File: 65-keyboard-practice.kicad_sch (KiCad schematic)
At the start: 3 parts

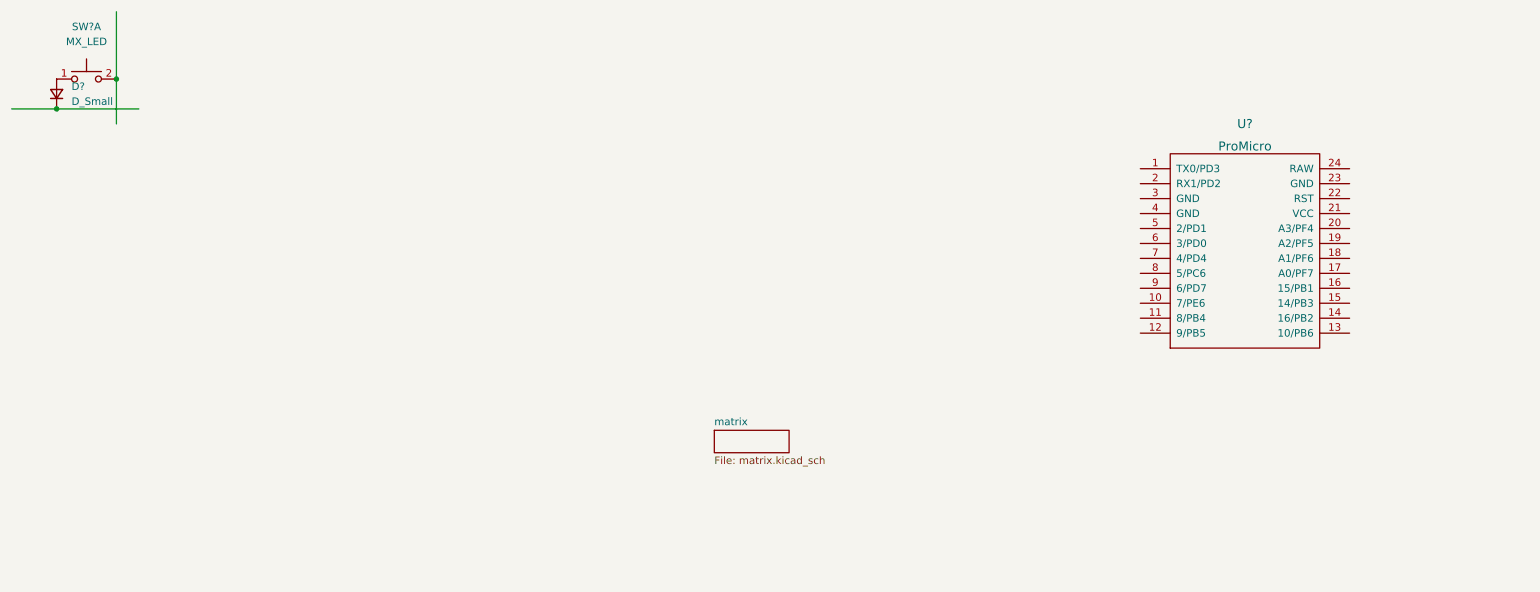
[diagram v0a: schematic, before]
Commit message: added GND and reset button to the promicro
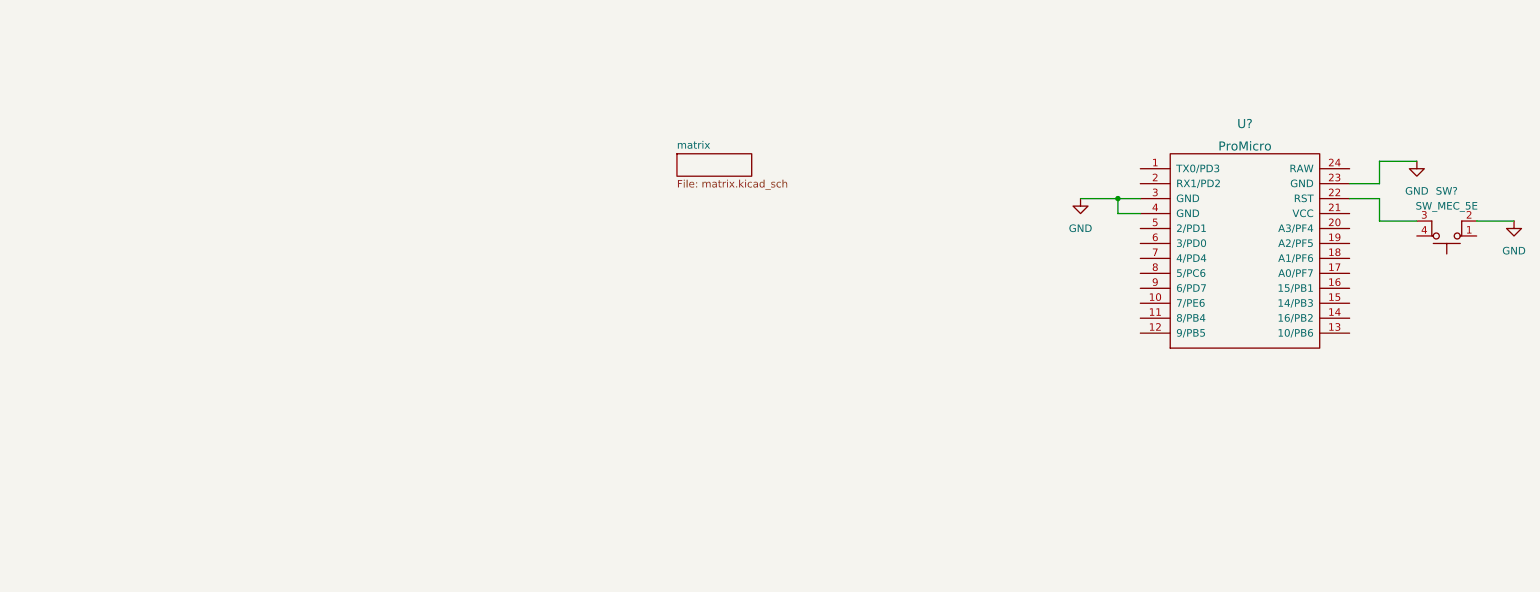
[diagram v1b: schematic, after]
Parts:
- removed D?: D_Small, symbol Device:D_Small
- removed SW?: MX_LED, symbol keebio:MX_LED
- added SW?: SW_MEC_5E, symbol Switch:SW_MEC_5E
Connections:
- net at U?.22 (RST): now also SW?.3 (K)
- net GND: now reaches U?.23 (GND)
- net GND: now also U?.3 (GND), U?.4 (GND), SW?.2
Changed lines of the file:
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@@
 (kicad_sch (version 20211123) (generator eeschema)
   (paper "A4")
-  (junction (at 40.64 38.1) (diameter 0) (color 0 0 0 0)
-  )
-  (junction (at 30.48 43.18) (diameter 0) (color 0 0 0 0)
-  )
-  (wire (pts (xy 22.86 43.18) (xy 30.48 43.18))
-    (stroke (width 0) (type default) (color 0 0 0 0))
-  )
-  (wire (pts (xy 30.48 43.18) (xy 44.45 43.18))
-    (stroke (width 0) (type default) (color 0 0 0 0))
-  )
-  (wire (pts (xy 40.64 26.67) (xy 40.64 38.1))
-    (stroke (width 0) (type default) (color 0 0 0 0))
-  )
-  (wire (pts (xy 40.64 38.1) (xy 40.64 45.72))
-    (stroke (width 0) (type default) (color 0 0 0 0))
-  )
-  (symbol (lib_id "keebio:MX_LED") (at 35.56 38.1 0) (unit 1)
+  (junction (at 210.82 58.42) (diameter 0) (color 0 0 0 0)
+  )
+  (wire (pts (xy 255.27 58.42) (xy 255.27 62.23))
+    (stroke (width 0) (type default) (color 0 0 0 0))
+  )
+  (wire (pts (xy 250.19 55.88) (xy 255.27 55.88))
+    (stroke (width 0) (type default) (color 0 0 0 0))
+  )
+  (wire (pts (xy 255.27 62.23) (xy 261.62 62.23))
+    (stroke (width 0) (type default) (color 0 0 0 0))
+  )
+  (wire (pts (xy 255.27 55.88) (xy 255.27 52.07))
+    (stroke (width 0) (type default) (color 0 0 0 0))
+  )
+  (wire (pts (xy 255.27 52.07) (xy 261.62 52.07))
+    (stroke (width 0) (type default) (color 0 0 0 0))
+  )
+  (wire (pts (xy 204.47 58.42) (xy 210.82 58.42))
+    (stroke (width 0) (type default) (color 0 0 0 0))
+  )
+  (wire (pts (xy 271.78 62.23) (xy 278.13 62.23))
+    (stroke (width 0) (type default) (color 0 0 0 0))
+  )
+  (wire (pts (xy 210.82 58.42) (xy 214.63 58.42))
+    (stroke (width 0) (type default) (color 0 0 0 0))
+  )
+  (wire (pts (xy 250.19 58.42) (xy 255.27 58.42))
+    (stroke (width 0) (type default) (color 0 0 0 0))
+  )
+  (wire (pts (xy 210.82 60.96) (xy 210.82 58.42))
+    (stroke (width 0) (type default) (color 0 0 0 0))
+  )
+  (wire (pts (xy 214.63 60.96) (xy 210.82 60.96))
+    (stroke (width 0) (type default) (color 0 0 0 0))
+  )
+  (symbol (lib_id "power:GND") (at 204.47 58.42 0) (unit 1)
     (in_bom yes) (on_board yes) (fields_autoplaced)
-    (property "Reference" "SW?" (id 0) (at 35.56 29.21 0))
-    (property "Value" "MX_LED" (id 1) (at 35.56 31.75 0))
-    (property "Footprint" "" (id 2) (at 35.56 38.1 0)
-      (effects (font (size 1.27 1.27)) hide)
-    )
-    (property "Datasheet" "" (id 3) (at 35.56 38.1 0)
+    (property "Reference" "#PWR?" (id 0) (at 204.47 64.77 0)
+      (effects (font (size 1.27 1.27)) hide)
+    )
+    (property "Value" "GND" (id 1) (at 204.47 63.5 0))
+    (property "Footprint" "" (id 2) (at 204.47 58.42 0)
+      (effects (font (size 1.27 1.27)) hide)
+    )
+    (property "Datasheet" "" (id 3) (at 204.47 58.42 0)
+      (effects (font (size 1.27 1.27)) hide)
+    )
+    (pin "1")
+  )
+  (symbol (lib_id "Switch:SW_MEC_5E") (at 266.7 62.23 180) (unit 1)
+    (in_bom yes) (on_board yes) (fields_autoplaced)
+    (property "Reference" "SW?" (id 0) (at 266.7 57.15 0))
+    (property "Value" "SW_MEC_5E" (id 1) (at 266.7 59.69 0))
+    (property "Footprint" "" (id 2) (at 266.7 69.85 0)
+      (effects (font (size 1.27 1.27)) hide)
+    )
+    (property "Datasheet" "http://www.apem.com/int/index.php?controller=attachment&id_attachment=1371" (id 3) (at 266.7 69.85 0)
       (effects (font (size 1.27 1.27)) hide)
     )
@@
     (pin "4")
   )
-  (symbol (lib_id "Device:D_Small") (at 30.48 40.64 90) (unit 1)
+  (symbol (lib_id "power:GND") (at 261.62 52.07 0) (unit 1)
     (in_bom yes) (on_board yes) (fields_autoplaced)
-    (property "Reference" "D?" (id 0) (at 33.02 39.3699 90)
-      (effects (font (size 1.27 1.27)) (justify right))
-    )
-    (property "Value" "D_Small" (id 1) (at 33.02 41.9099 90)
-      (effects (font (size 1.27 1.27)) (justify right))
-    )
-    (property "Footprint" "" (id 2) (at 30.48 40.64 90)
-      (effects (font (size 1.27 1.27)) hide)
-    )
-    (property "Datasheet" "~" (id 3) (at 30.48 40.64 90)
+    (property "Reference" "#PWR?" (id 0) (at 261.62 58.42 0)
+      (effects (font (size 1.27 1.27)) hide)
+    )
+    (property "Value" "GND" (id 1) (at 261.62 57.15 0))
+    (property "Footprint" "" (id 2) (at 261.62 52.07 0)
+      (effects (font (size 1.27 1.27)) hide)
+    )
+    (property "Datasheet" "" (id 3) (at 261.62 52.07 0)
       (effects (font (size 1.27 1.27)) hide)
     )
     (pin "1")
-    (pin "2")
   )
   (symbol (lib_id "keebio:ProMicro") (at 232.41 67.31 0) (unit 1)
@@
     (pin "9")
   )
-  (sheet (at 142.24 97.79) (size 12.7 3.81) (fields_autoplaced)
+  (symbol (lib_id "power:GND") (at 278.13 62.23 0) (unit 1)
+    (in_bom yes) (on_board yes) (fields_autoplaced)
+    (property "Reference" "#PWR?" (id 0) (at 278.13 68.58 0)
+      (effects (font (size 1.27 1.27)) hide)
+    )
+    (property "Value" "GND" (id 1) (at 278.13 67.31 0))
+    (property "Footprint" "" (id 2) (at 278.13 62.23 0)
+      (effects (font (size 1.27 1.27)) hide)
+    )
+    (property "Datasheet" "" (id 3) (at 278.13 62.23 0)
+      (effects (font (size 1.27 1.27)) hide)
+    )
+    (pin "1")
+  )
+  (sheet (at 135.89 50.8) (size 12.7 3.81) (fields_autoplaced)
     (stroke (width 0.1524) (type solid) (color 0 0 0 0))
     (fill (color 0 0 0 0.0000))
-    (property "Sheet name" "matrix" (id 0) (at 142.24 97.0784 0)
+    (property "Sheet name" "matrix" (id 0) (at 135.89 50.0884 0)
       (effects (font (size 1.27 1.27)) (justify left bottom))
     )
-    (property "Sheet file" "matrix.kicad_sch" (id 1) (at 142.24 102.1846 0)
+    (property "Sheet file" "matrix.kicad_sch" (id 1) (at 135.89 55.1946 0)
       (effects (font (size 1.27 1.27)) (justify left top))
     )
@@
   )
   (symbol_instances
+    (path "/73fcfd8a-9610-4862-8758-a9cb100236aa"
+      (reference "#PWR?") (unit 1) (value "GND") (footprint "")
+    )
+    (path "/9c7935a6-744f-46b1-a276-27252c39d402"
+      (reference "#PWR?") (unit 1) (value "GND") (footprint "")
+    )
+    (path "/f2ebe5e8-f267-4b40-9cca-169b4324c72b"
+      (reference "#PWR?") (unit 1) (value "GND") (footprint "")
+    )
     (path "/c4ed3659-6d37-44a6-b5ca-7e464c3558fc/0189b339-e276-445f-84b3-11fa3e094def"
       (reference "D?") (unit 1) (value "D_Small") (footprint "")
@@
       (reference "D?") (unit 1) (value "D_Small") (footprint "")
     )
-    (path "/b217ac5c-bb08-4598-80a1-f708d8012252"
-      (reference "D?") (unit 1) (value "D_Small") (footprint "")
-    )
     (path "/c4ed3659-6d37-44a6-b5ca-7e464c3558fc/b26f658e-15d8-48fa-af25-636915254238"
       (reference "D?") (unit 1) (value "D_Small") (footprint "")
@@
       (reference "SW?") (unit 1) (value "MX_LED") (footprint "")
     )
-    (path "/7689c30f-813f-42a7-ad77-22c5cfc89d79"
-      (reference "SW?") (unit 1) (value "MX_LED") (footprint "")
+    (path "/76c93b00-4581-47e2-860e-798daded2dfe"
+      (reference "SW?") (unit 1) (value "SW_MEC_5E") (footprint "")
     )
     (path "/c4ed3659-6d37-44a6-b5ca-7e464c3558fc/855e7ffd-9a29-4ac3-92c9-7962e6bb0d8f"

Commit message: added some submodules
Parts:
- gave numbers to parts that had none: 2

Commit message: half wiring done
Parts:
- SW1: footprint (none) -> random-keyboard-parts:PushButton_6x6mm_TH
- U1: footprint (none) -> Keebio-Parts:ArduinoProMicro

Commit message: Finished the design
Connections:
- net COL1: now reaches U1.10 (7/PE6)
- net COL2: now reaches U1.11 (8/PB4)
- net COL3: now reaches U1.12 (9/PB5)
- net COL4: now reaches U1.13 (10/PB6)
- net COL5: now reaches U1.14 (16/PB2)
- net COL6: now reaches U1.15 (14/PB3)
- net COL7: now reaches U1.16 (15/PB1)
- net ROW4: now reaches U1.17 (A0/PF7)
- net ROW3: now reaches U1.5 (2/PD1)
- net ROW2: now reaches U1.6 (3/PD0)
- net ROW0: now reaches U1.7 (4/PD4)
- net ROW1: now reaches U1.8 (5/PC6)
- net COL0: now reaches U1.9 (6/PD7)
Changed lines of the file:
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@@
     (stroke (width 0) (type default) (color 0 0 0 0))
+  )
+  (global_label "ROW1" (shape input) (at 214.63 71.12 180) (fields_autoplaced)
+    (effects (font (size 1.27 1.27)) (justify right))
+    (property "Intersheet References" "${INTERSHEET_REFS}" (id 0) (at 206.9555 71.0406 0)
+      (effects (font (size 1.27 1.27)) (justify right) hide)
+    )
+  )
+  (global_label "ROW4" (shape input) (at 250.19 71.12 0) (fields_autoplaced)
+    (effects (font (size 1.27 1.27)) (justify left))
+    (property "Intersheet References" "${INTERSHEET_REFS}" (id 0) (at 257.8645 71.0406 0)
+      (effects (font (size 1.27 1.27)) (justify left) hide)
+    )
+  )
+  (global_label "COL0" (shape input) (at 214.63 73.66 180) (fields_autoplaced)
+    (effects (font (size 1.27 1.27)) (justify right))
+    (property "Intersheet References" "${INTERSHEET_REFS}" (id 0) (at 207.3788 73.5806 0)
+      (effects (font (size 1.27 1.27)) (justify right) hide)
+    )
+  )
+  (global_label "COL2" (shape input) (at 214.63 78.74 180) (fields_autoplaced)
+    (effects (font (size 1.27 1.27)) (justify right))
+    (property "Intersheet References" "${INTERSHEET_REFS}" (id 0) (at 207.3788 78.6606 0)
+      (effects (font (size 1.27 1.27)) (justify right) hide)
+    )
+  )
+  (global_label "ROW0" (shape input) (at 214.63 68.58 180) (fields_autoplaced)
+    (effects (font (size 1.27 1.27)) (justify right))
+    (property "Intersheet References" "${INTERSHEET_REFS}" (id 0) (at 206.9555 68.5006 0)
+      (effects (font (size 1.27 1.27)) (justify right) hide)
+    )
+  )
+  (global_label "COL3" (shape input) (at 214.63 81.28 180) (fields_autoplaced)
+    (effects (font (size 1.27 1.27)) (justify right))
+    (property "Intersheet References" "${INTERSHEET_REFS}" (id 0) (at 207.3788 81.2006 0)
+      (effects (font (size 1.27 1.27)) (justify right) hide)
+    )
+  )
+  (global_label "COL1" (shape input) (at 214.63 76.2 180) (fields_autoplaced)
+    (effects (font (size 1.27 1.27)) (justify right))
+    (property "Intersheet References" "${INTERSHEET_REFS}" (id 0) (at 207.3788 76.1206 0)
+      (effects (font (size 1.27 1.27)) (justify right) hide)
+    )
+  )
+  (global_label "COL4" (shape input) (at 250.19 81.28 0) (fields_autoplaced)
+    (effects (font (size 1.27 1.27)) (justify left))
+    (property "Intersheet References" "${INTERSHEET_REFS}" (id 0) (at 257.4412 81.2006 0)
+      (effects (font (size 1.27 1.27)) (justify left) hide)
+    )
+  )
+  (global_label "ROW3" (shape input) (at 214.63 63.5 180) (fields_autoplaced)
+    (effects (font (size 1.27 1.27)) (justify right))
+    (property "Intersheet References" "${INTERSHEET_REFS}" (id 0) (at 206.9555 63.4206 0)
+      (effects (font (size 1.27 1.27)) (justify right) hide)
+    )
+  )
+  (global_label "COL5" (shape input) (at 250.19 78.74 0) (fields_autoplaced)
+    (effects (font (size 1.27 1.27)) (justify left))
+    (property "Intersheet References" "${INTERSHEET_REFS}" (id 0) (at 257.4412 78.6606 0)
+      (effects (font (size 1.27 1.27)) (justify left) hide)
+    )
+  )
+  (global_label "COL7" (shape input) (at 250.19 73.66 0) (fields_autoplaced)
+    (effects (font (size 1.27 1.27)) (justify left))
+    (property "Intersheet References" "${INTERSHEET_REFS}" (id 0) (at 257.4412 73.5806 0)
+      (effects (font (size 1.27 1.27)) (justify left) hide)
+    )
+  )
+  (global_label "ROW2" (shape input) (at 214.63 66.04 180) (fields_autoplaced)
+    (effects (font (size 1.27 1.27)) (justify right))
+    (property "Intersheet References" "${INTERSHEET_REFS}" (id 0) (at 206.9555 65.9606 0)
+      (effects (font (size 1.27 1.27)) (justify right) hide)
+    )
+  )
+  (global_label "COL6" (shape input) (at 250.19 76.2 0) (fields_autoplaced)
+    (effects (font (size 1.27 1.27)) (justify left))
+    (property "Intersheet References" "${INTERSHEET_REFS}" (id 0) (at 257.4412 76.1206 0)
+      (effects (font (size 1.27 1.27)) (justify left) hide)
+    )
   )
   (symbol (lib_id "power:GND") (at 204.47 58.42 0) (unit 1)

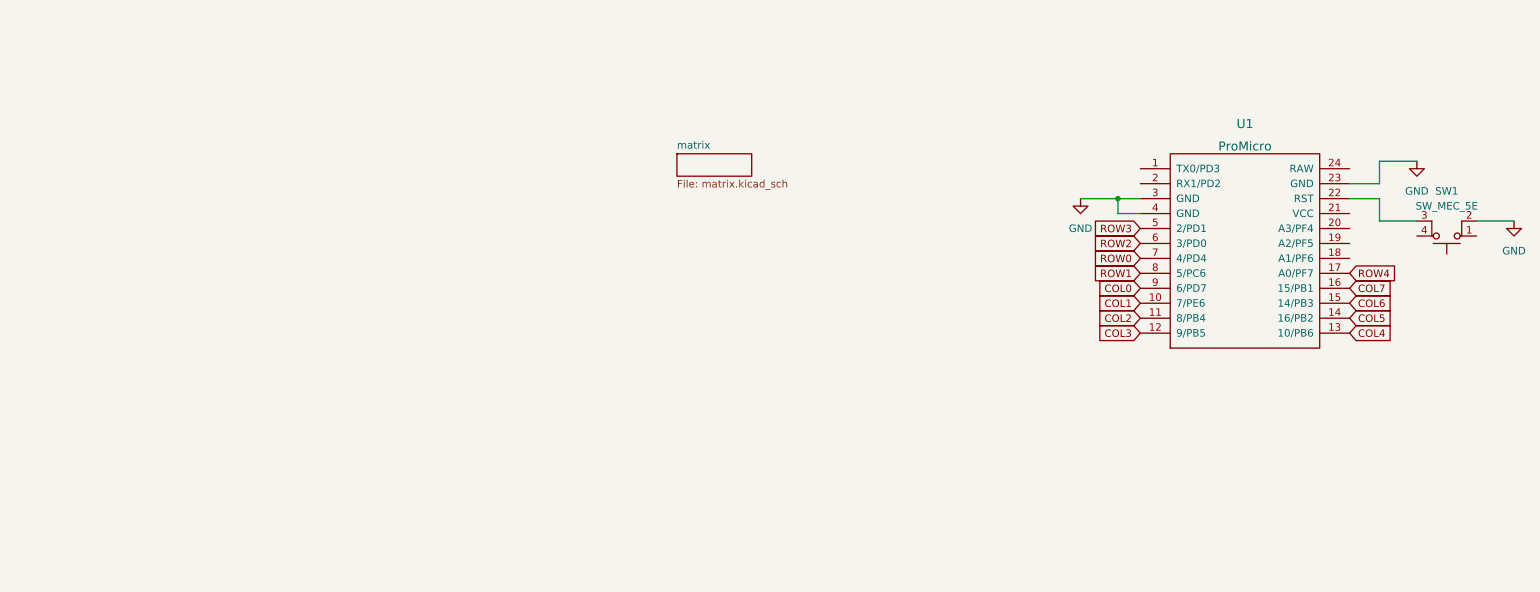
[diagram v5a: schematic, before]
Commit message: Added rgb underglow
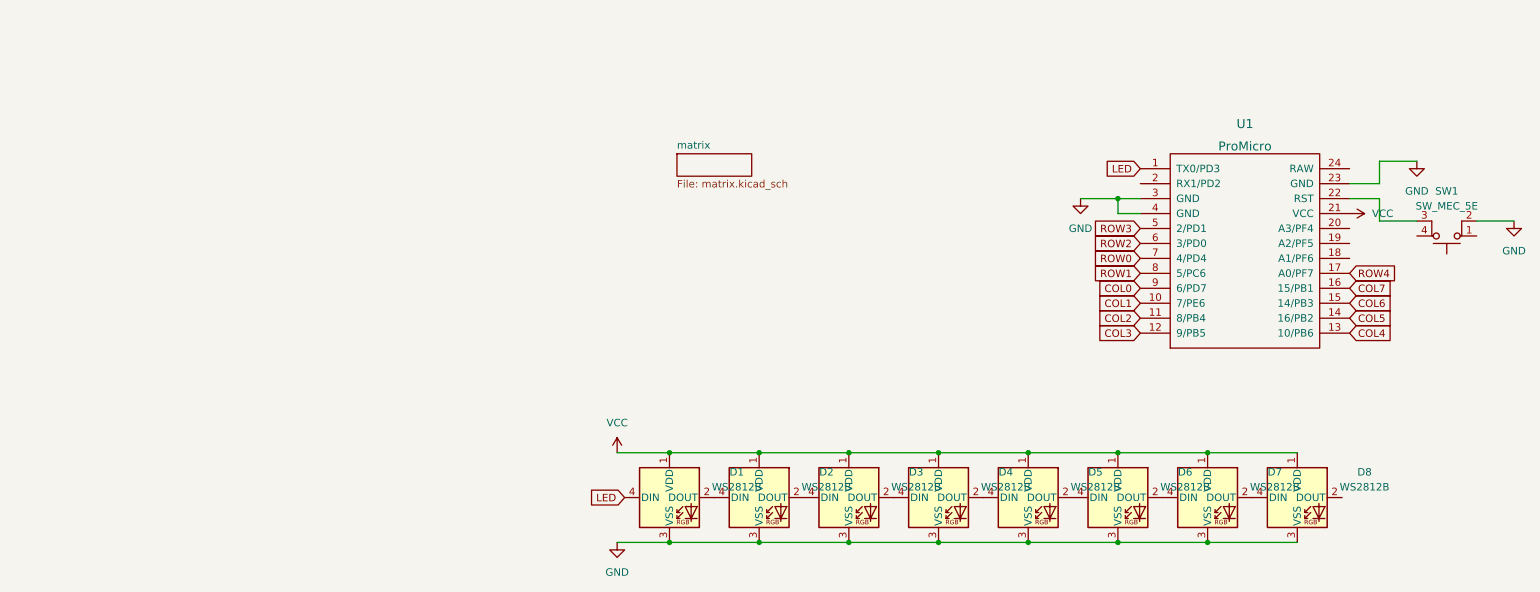
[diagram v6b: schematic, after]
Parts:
- added D1, D2, D3, D4, D5, D6, D7, D8: WS2812B, LED_SMD:LED_WS2812B_PLCC4_5.0x5.0mm_P3.2mm, symbol LED:WS2812B
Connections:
- net GND: now also D1.3 (VSS), D2.3 (VSS), D3.3 (VSS), D4.3 (VSS), D5.3 (VSS), D6.3 (VSS), D7.3 (VSS), D8.3 (VSS)
- net LED: now reaches U1.1 (TX0/PD3)
- net LED: now also D1.4 (DIN)
- net VCC: now reaches U1.21 (VCC)
- net VCC: now also D1.1 (VDD), D2.1 (VDD), D3.1 (VDD), D4.1 (VDD), D5.1 (VDD), D6.1 (VDD), D7.1 (VDD), D8.1 (VDD)
- new net: D6.2 (DOUT), D7.4 (DIN)
- new net: D5.2 (DOUT), D6.4 (DIN)
- new net: D4.2 (DOUT), D5.4 (DIN)
- new net: D3.2 (DOUT), D4.4 (DIN)
- new net: D2.2 (DOUT), D3.4 (DIN)
- new net: D1.2 (DOUT), D2.4 (DIN)
- new net: D7.2 (DOUT), D8.4 (DIN)
